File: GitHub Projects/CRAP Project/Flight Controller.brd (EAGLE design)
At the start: 40 x 95 mm, 138 parts, among them J1 2POS_SCREWTERM, J101 2POS_SCREWTERM, J2 4POS_SCREWTERM, J3 4POS_SCREWTERM, J4 4POS_SCREWTERM, J5 4POS_SCREWTERM, Q101 IPD042P03L3G, Q102 IPD042P03L3G, Q1101 PMF170XP, Q1102 DMG4800LSD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

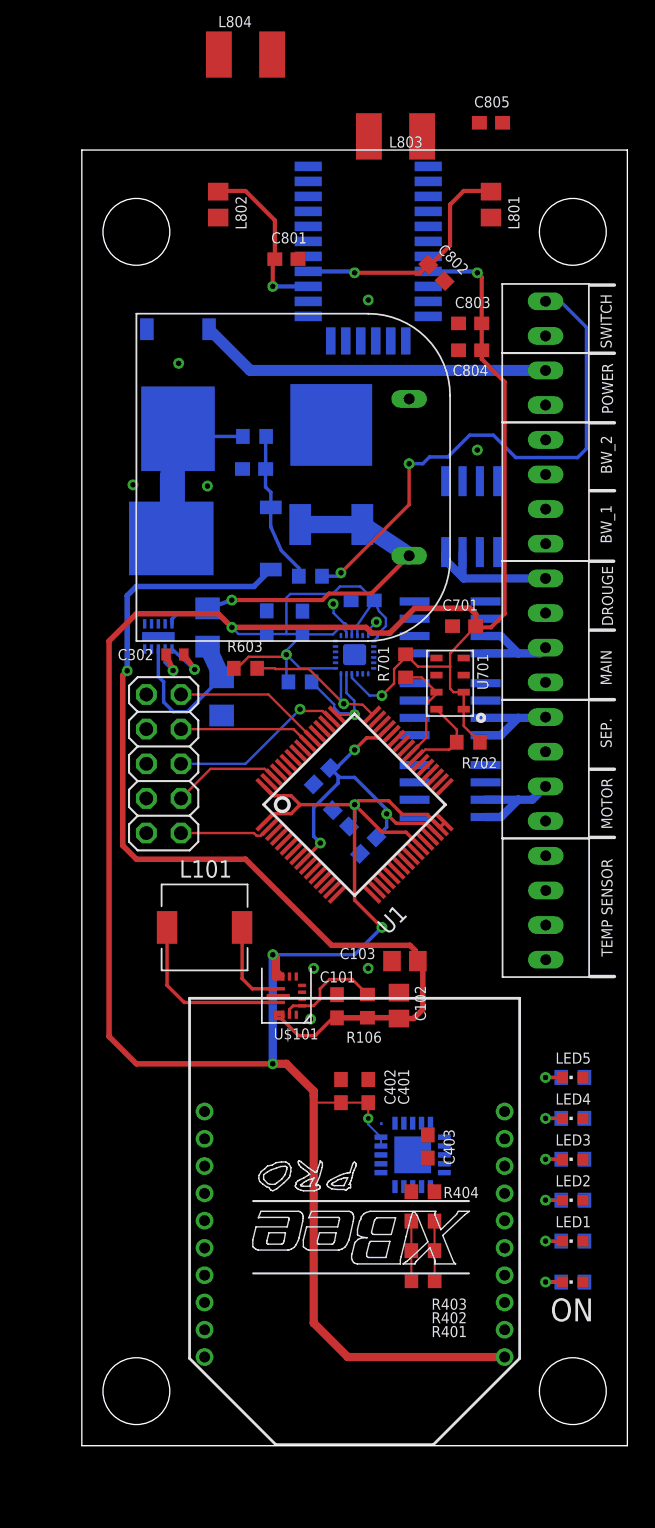
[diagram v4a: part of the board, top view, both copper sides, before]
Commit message: Minor Changes to some routing
Having problems with using the alternate grid.  Routing engine will not
allow me to route on the alternate grid, which has stopped progress for
the time being.
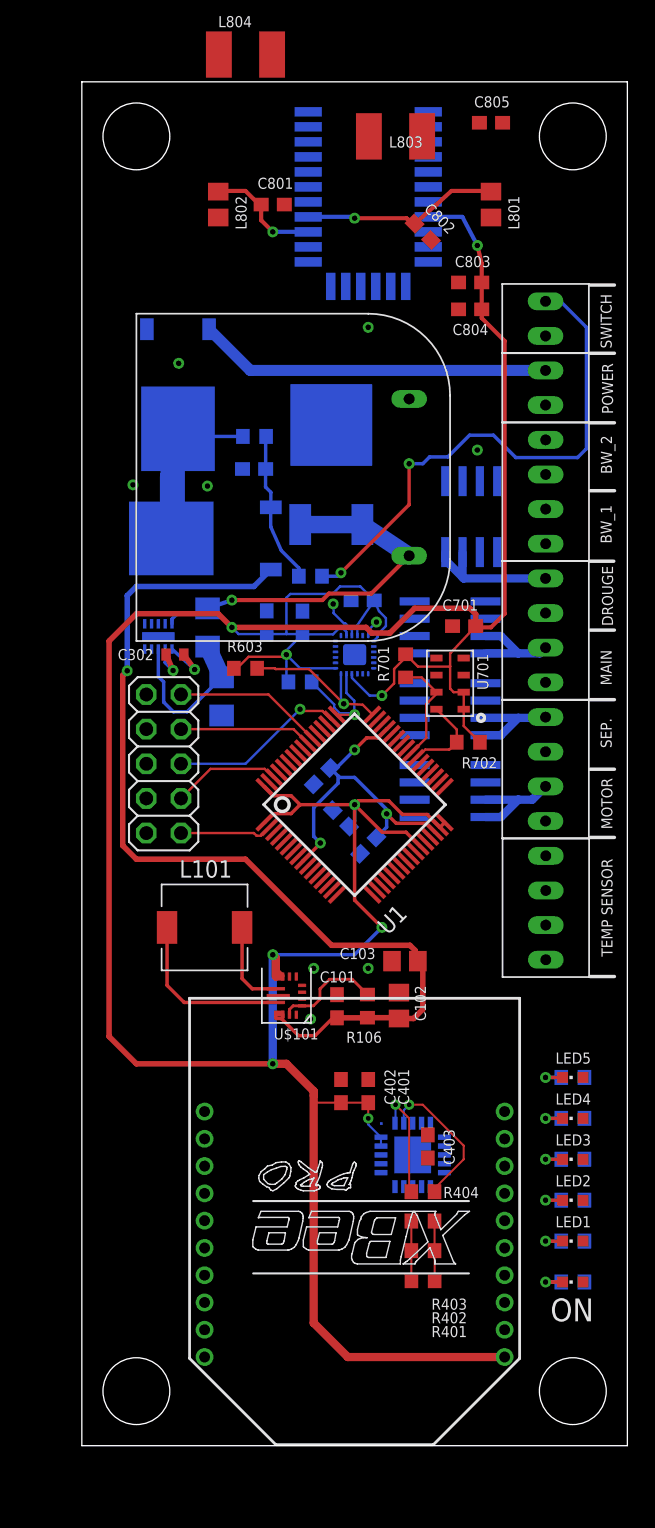
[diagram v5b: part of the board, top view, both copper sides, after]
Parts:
- U1: value (none) -> G55J19
- U301: value (none) -> LTC3225
- U601: value (none) -> MPU9250
- U701: value (none) -> MS5611
- moved C801 4.12 mm to (14.0, 91.0)
- moved U$801 4.00 mm to (21.0, 85.0)
- moved C802 3.16 mm to (25.0, 89.0)
- moved C803 3.00 mm to (28.5, 85.3)
- moved C804 3.00 mm to (28.5, 83.3)
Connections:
- new net BREAKWIRE1:+3V3: R901.2
- new net BREAKWIRE2:+3V3: R1001.2
- new net HIGH_G1:+3V3: C201.1, C202.1, C203.1, U201.P1, U201.P14, U201.P15
- net +3V3: no longer C201.1, C202.1, C203.1, R1001.2, R901.2, U201.P1, U201.P14, U201.P15
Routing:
- net RTD:N$5: track 0.00 -> 11.0 mm, vias 0 -> 1
- net RTD:N$1: track 4.37 -> 12.6 mm, vias 0 -> 1
- net GPS1:N$3: track 12.6 -> 8.57 mm
- net GPS1:N$2: track 17.7 -> 14.5 mm
- net +3V3: track 262.8 -> 265.9 mm
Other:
- board size 40 x 95 mm -> 40 x 100 mm

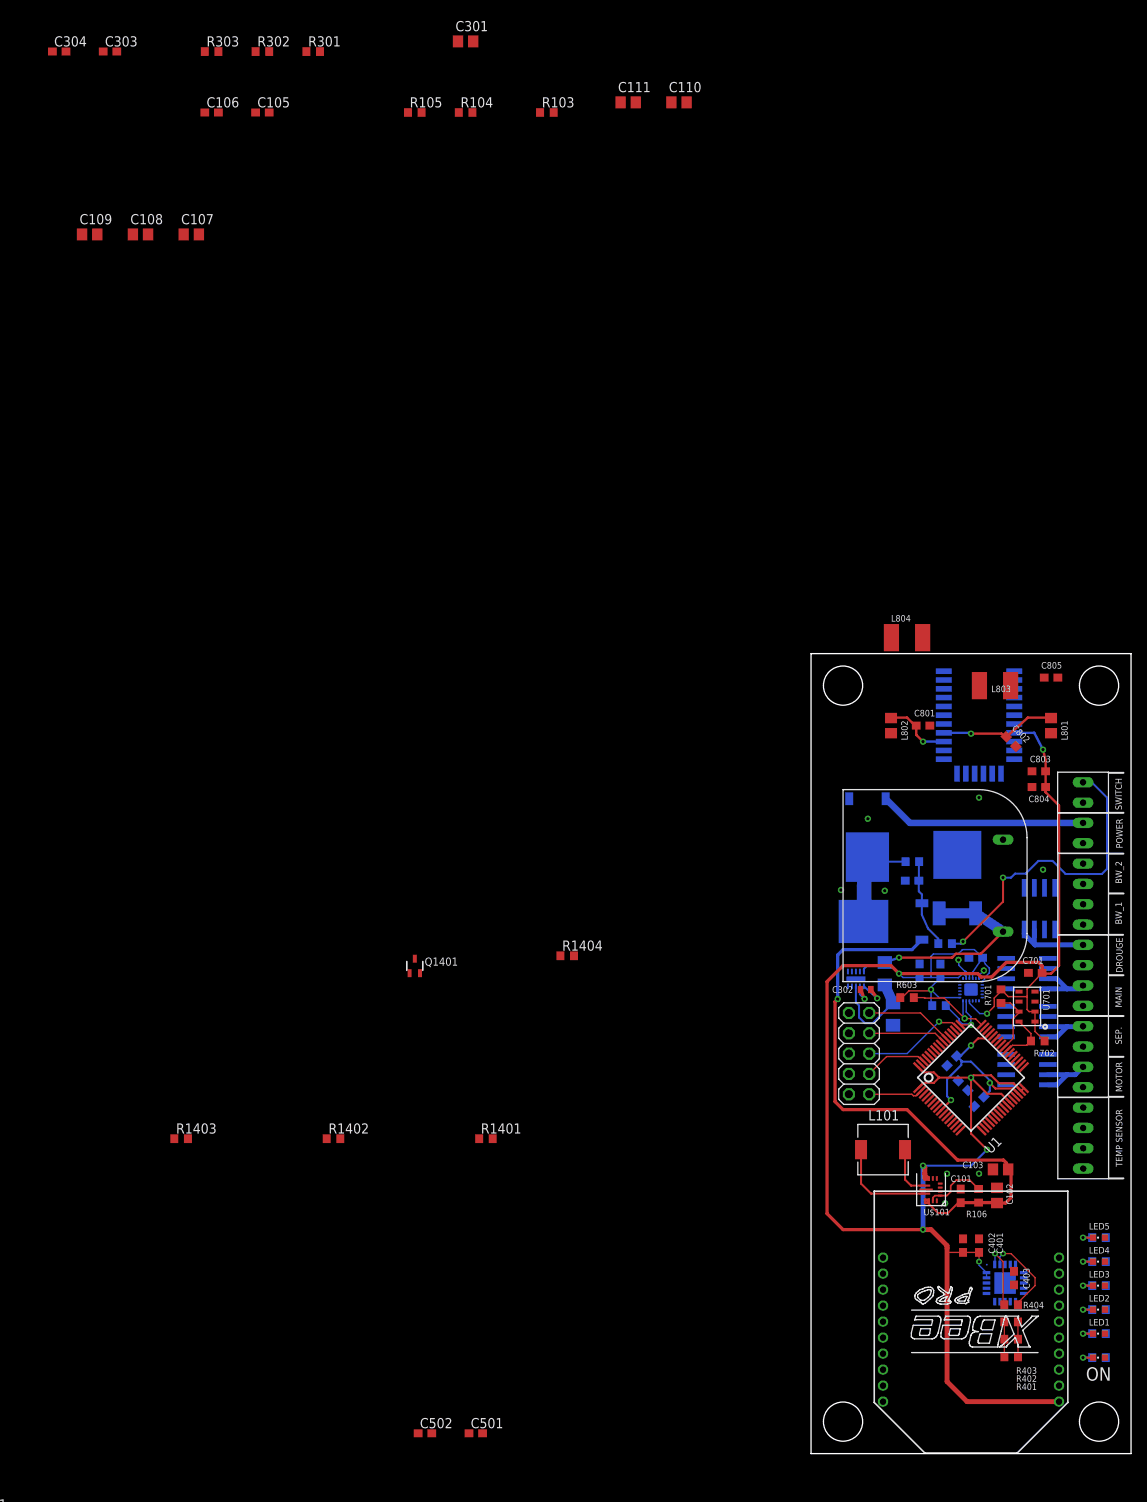
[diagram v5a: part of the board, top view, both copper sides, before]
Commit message: Major revisions
1. Made board 30mm taller to allow for more space in cramped enviroment.
Deemed absolutely critical.
2. Majorly changed the power turn-on and turn-off MOSFETs design and
location to clear up room in the mid-board area
3. Moved the super capacitor nearer to the top of the extended section,
and also made it have a verticle orientation; should allow for better
handling of vertical Gs
4. Moved the super-capacitor charging circuitry in the extra space under
the super-cap.  Fits nicely in a small area now.
5. Created Vishay.lbr, Adafruit.lbr, nkk.lbr, and semtech.lbr
6. Added common SMT pads to Semtech.lbr and Vishay.lbr
7. Created MOSFETs in Vishay.lbr
8.Created MOSFETs in semtech.lbr
9. Completely routed the GPS and passives; just needs UART connections
to the uC now
10. Changed the DRC (Design Rules) to better reflect the capabilities of
Advanced Circuit's $33/board abilities.  Changes are mostly downsizing
the rules to 7mil of smallest hole, trace, and spacing between copper to
copper
11. Modified all vias in tight locations and low power consumption roles
to be a 7mil (0.18mm, rounded) drill hole
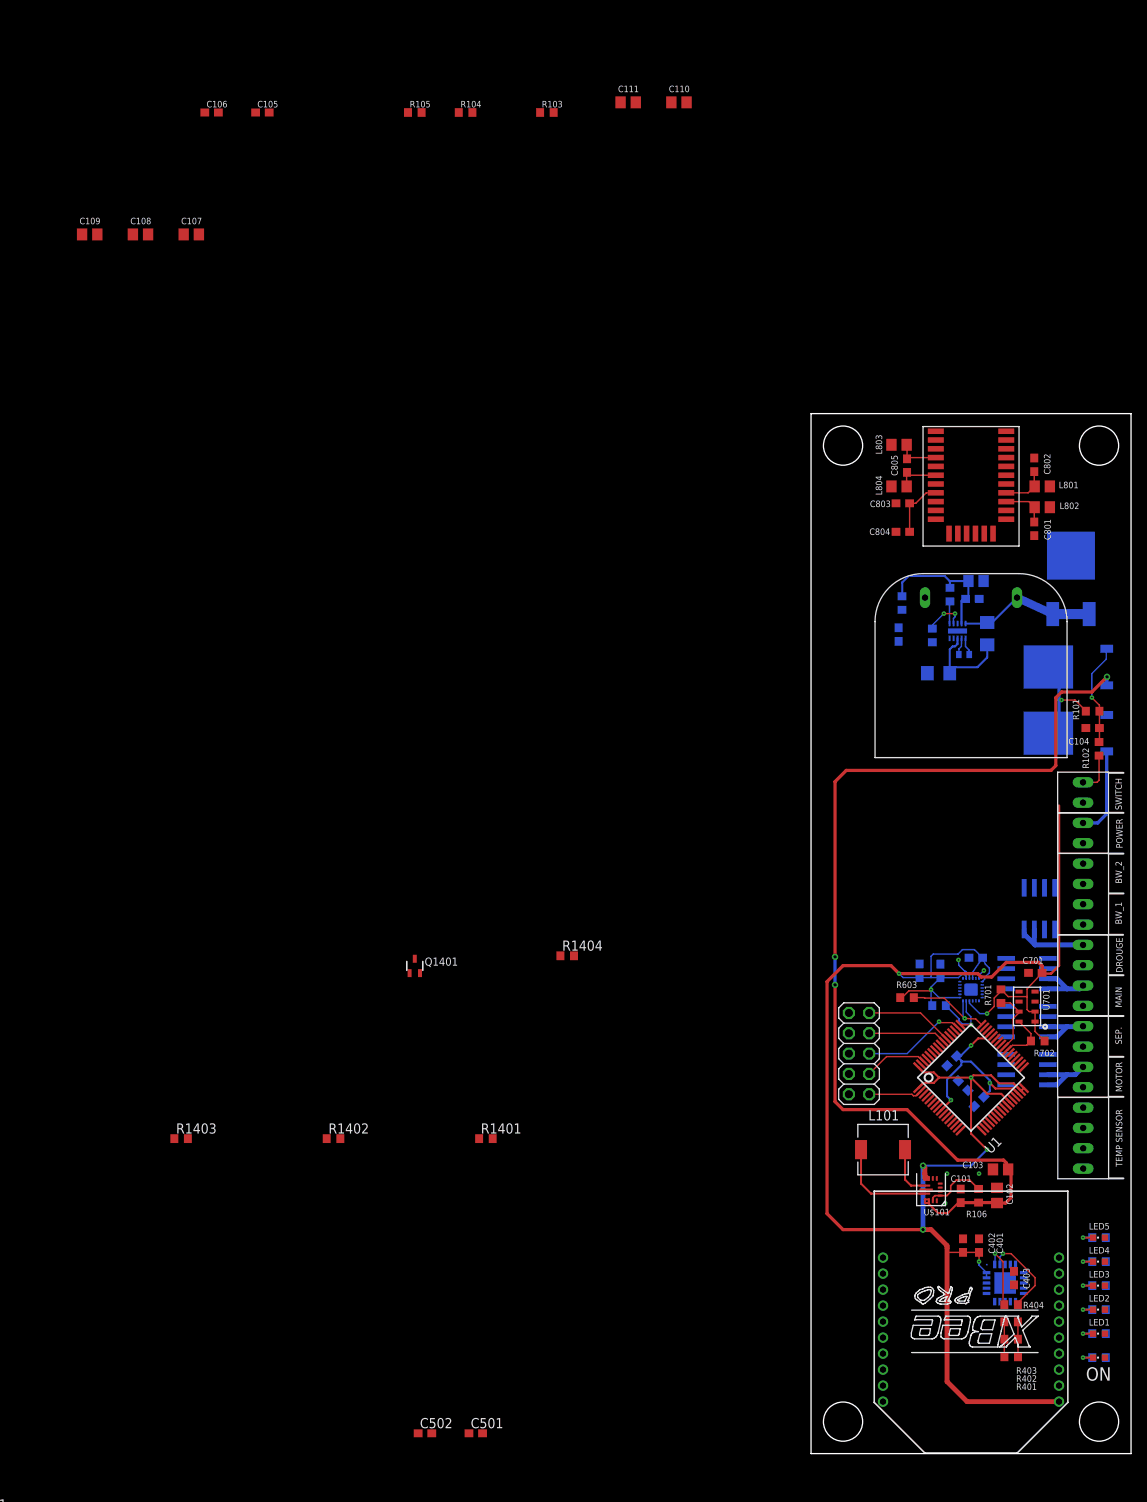
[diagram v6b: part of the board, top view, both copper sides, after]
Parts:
- L803, L804: device rcl:L1812 -> rcl:R0805
- moved C304 127.7 mm to (10.9, 102.4), flipped to the bottom, turned to 270 degrees
- moved C303 127.7 mm to (20.2, 106.8), flipped to the bottom, turned to 180 degrees
- moved R303 115.9 mm to (15.2, 102.3), flipped to the bottom, turned to 90 degrees
- moved R302 105.6 mm to (11.4, 106.3), flipped to the bottom, turned to 90 degrees
- moved R301 104.6 mm to (17.4, 107.4), flipped to the bottom, turned to 90 degrees
- moved C301 92.9 mm to (20.6, 109.1), flipped to the bottom, turned to 180 degrees
- moved U301 45.3 mm to (17.3, 103.8)
- moved C306 44.4 mm to (22.0, 102.5)
- moved C302 43.6 mm to (19.1, 99.9), flipped to the bottom, turned to 0 degrees
- moved C307 43.0 mm to (15.9, 97.5), turned to 0 degrees
- moved D301 40.0 mm to (32.5, 109.7)
- moved Q102 39.3 mm to (32.2, 98.3)
- moved C803 37.6 mm to (11.5, 118.8)
- moved C305 36.2 mm to (20.0, 107.0), turned to 180 degrees
- moved C804 36.1 mm to (11.5, 115.2)
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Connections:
- net DCDC_REGULATOR:N$2 renamed DCDC_REGULATOR:N$1
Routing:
- net DCDC_REGULATOR:VIN: track 72.1 -> 127.3 mm, vias 1 -> 3
- net DCDC_REGULATOR:N$6: track 39.1 -> 5.19 mm, vias 2 -> 0
- net VCC_IN: track 25.9 -> 11.2 mm
- net +3V3: track 265.9 -> 280.0 mm, vias 9 -> 8
- net ORDNANCE_POWER:N$3: track 28.2 -> 17.3 mm, vias 1 -> 0
- net GPS1:N$2: track 14.5 -> 5.75 mm, vias 1 -> 0
- net DCDC_REGULATOR:N$1: track 21.3 -> 12.9 mm, vias 0 -> 1
- net GPS1:N$4: track 0.00 -> 5.75 mm
- net GPS1:N$1: track 0.00 -> 5.55 mm
- net ORDNANCE_POWER:N$6: track 0.00 -> 5.20 mm, vias 0 -> 2
- net GPS1:N$3: track 8.57 -> 5.74 mm, vias 1 -> 0
- net ORDNANCE_POWER:N$5: track 0.00 -> 2.78 mm
- net DCDC_REGULATOR:N$4: track 11.1 -> 12.8 mm, vias 0 -> 1
- net ORDNANCE_POWER:N$1: track 3.59 -> 2.21 mm, vias 1 -> 0
- net ORDNANCE_POWER:N$2: track 3.09 -> 2.15 mm, vias 1 -> 0
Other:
- board size 40 x 100 mm -> 40 x 130 mm

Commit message: Routing of high-g IMU, regular IMU, firing circuits
1. Chose communication lines for all sensors and memory to the uC
2. Routed 100% the MPU9250
3. Routed 100% the high-g accelerometer
4. Routed 100% the breakwire circuits
5. Routed 75% of the firing circuits
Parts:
- removed R1: 10k, rcl:R0603
- moved R1105 432.5 mm to (37.2, 62.3), flipped to the bottom, turned to 270 degrees
- moved R1205 375.6 mm to (37.2, 57.2), flipped to the bottom, turned to 270 degrees
- moved R1305 320.8 mm to (37.2, 52.3), flipped to the bottom, turned to 270 degrees
- moved C203 258.6 mm to (15.8, 66.3), turned to 180 degrees
- moved C202 258.5 mm to (24.8, 64.5), turned to 270 degrees
- moved U201 250.2 mm to (20.0, 70.0), turned to 180 degrees
- moved C201 249.3 mm to (15.3, 64.0), turned to 180 degrees
- moved R1405 195.4 mm to (37.2, 47.1), flipped to the bottom, turned to 270 degrees
- moved D901 177.9 mm to (30.1, 70.0), flipped to the bottom
- moved D1001 175.8 mm to (30.1, 71.5), flipped to the bottom
- moved C1001 175.5 mm to (37.2, 72.5), flipped to the bottom, turned to 270 degrees
- moved C901 174.8 mm to (37.2, 67.3), flipped to the bottom, turned to 270 degrees
- moved R901 164.5 mm to (26.7, 70.4), flipped to the bottom
- moved R1001 162.9 mm to (26.7, 72.5), flipped to the bottom
- moved MEMORY1:U1 140.3 mm to (11.1, 78.0), flipped to the bottom, turned to 270 degrees
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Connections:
- removed net HIGH_G1:+3V3: C201.1, C202.1, C203.1, U201.P1, U201.P14, U201.P15
- removed net HIGH_G1:CS: U201.P8
- removed net HIGH_G1:SCL/SPC: U201.P4
- removed net HIGH_G1:SDA/SDI: U201.P6
- removed net MEMORY1:+3V3: MEMORY1:C1.1, MEMORY1:U1.2
- removed net MEMORY1:GND: MEMORY1:C1.2, MEMORY1:U1.10
- removed net MPU9250_SCL: R602.1, U1.49, U601.23
- removed net MPU9250_SDA: R603.1, U1.48, U601.24
- removed net N$14: R1.2, U601.9
- removed net N$20: U1.8
- removed net N$21: U1.17
- removed net RTD:!CS: U$401.13
- removed net RTD:SCLK: U$401.12
- removed net RTD:SDI: U$401.11
- removed net RTD:SDO: U$401.14
- new net IMU_SCL: R602.1, U1.49, U201.P4, U601.23
- new net IMU_SDA: R603.1, U1.48, U201.P6, U601.24
- new net MEM_!CS: MEMORY1:U1.7, U1.15
- new net MEM_MISO: MEMORY1:U1.8, U1.4
- new net MEM_MOSI: MEMORY1:U1.15, U1.5
- new net MEM_SCK: MEMORY1:U1.16, U1.57
- new net RTD_!CS: U$401.13, U1.18
- new net RTD_MISO: U$401.14, U1.8
- new net RTD_MOSI: U$401.11, U1.17
- new net RTD_SCK: U$401.12, U1.22
- net +3V3: now also C201.1, C202.1, C203.1, MEMORY1:C1.1, MEMORY1:U1.2, U201.P1, U201.P14, U201.P15, U201.P8, U601.9
- net GND: now also MEMORY1:C1.2, MEMORY1:U1.10; no longer R1.1
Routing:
- net +12V: track 0.00 -> 40.3 mm
- net IMU_SDA: track 0.00 -> 30.8 mm, vias 0 -> 4
- net IMU_SCL: track 0.00 -> 28.0 mm, vias 0 -> 2
- net MPU9250_SDA: track 12.1 -> 0.00 mm, vias 1 -> 0
- net MPU9250_SCL: track 8.85 -> 0.00 mm, vias 1 -> 0
- net FIRING_CIRCUIT3:N$1: track 0.00 -> 8.71 mm
- net FIRING_CIRCUIT2:N$1: track 0.00 -> 8.71 mm
- net FIRING_CIRCUIT4:N$1: track 0.00 -> 8.71 mm
- net FIRING_CIRCUIT1:N$1: track 0.00 -> 8.71 mm
- net +3V3: track 280.0 -> 273.4 mm, vias 8 -> 10
- net N$13: track 0.00 -> 5.85 mm
- net FC1-2: track 7.50 -> 11.0 mm
- net FC1-: track 7.73 -> 11.2 mm
- net N$11: track 0.00 -> 3.43 mm
- net N$10: track 0.00 -> 3.41 mm
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
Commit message: More routing and schematic changes
1. Finished 100% the schematic of all misc. connections that were going
to things, such as all comms, all LED indication pins, and all
enable/disable pins
2. Added FTDI FT232R for serial to USB connectivity
3. Routed the power line for the firing circuit from supercap
4. Routed LED indication
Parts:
- added R304: 10k, resistor:R0603
- LED1, LED2, LED3, LED4, LED5: value (none) -> BLUE
- ON: value (none) -> RED
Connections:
- removed net FC1-1: C1301.1, J3.4, Q1302.7, Q1302.8, R1305.1
- removed net FC1-2: C1201.1, J4.2, Q1202.7, Q1202.8, R1205.1
- removed net FC1-3: C1101.1, J4.4, Q1102.7, Q1102.8, R1105.1
- removed net FIRING_CIRCUIT1:!CONT_EN: Q1401.2, R1404.1
- removed net FIRING_CIRCUIT1:FIRE1: Q1402.2, R1403.2
- removed net FIRING_CIRCUIT1:FIRE2: Q1402.4, R1402.2
- removed net FIRING_CIRCUIT2:!CONT_EN: Q1301.2, R1304.1
- removed net FIRING_CIRCUIT2:FIRE1: Q1302.2, R1303.2
- removed net FIRING_CIRCUIT2:FIRE2: Q1302.4, R1302.2
- removed net FIRING_CIRCUIT3:!CONT_EN: Q1201.2, R1204.1
- removed net FIRING_CIRCUIT3:FIRE1: Q1202.2, R1203.2
- removed net FIRING_CIRCUIT3:FIRE2: Q1202.4, R1202.2
- removed net FIRING_CIRCUIT4:!CONT_EN: Q1101.2, R1104.1
- removed net FIRING_CIRCUIT4:FIRE1: Q1102.2, R1103.2
- removed net FIRING_CIRCUIT4:FIRE2: Q1102.4, R1102.2
- removed net N$10: C901.1, J5.2
- removed net N$12: C1001.1, J5.4
- removed net ORDNANCE_POWER:!SHDN: U301.P4
- new net BW1_STATUS: C901.1, J5.2, U1.46
- new net BW2_STATUS: C1001.1, J5.4, U1.47
- new net FC1_!CONT_EN: Q1401.2, R1404.1, U1.6
- new net FC1_FIRE: Q1402.2, Q1402.4, R1402.2, R1403.2, U1.7
- new net FC2-: C1301.1, J3.4, Q1302.7, Q1302.8, R1305.1, U1.52
- new net FC2_!CONT_EN: Q1301.2, R1304.1, U1.61
- new net FC2_FIRE: Q1302.2, Q1302.4, R1302.2, R1303.2, U1.11
- new net FC3-: C1201.1, J4.2, Q1202.7, Q1202.8, R1205.1, U1.19
- new net FC3_!CONT_EN: Q1201.2, R1204.1, U1.12
- new net FC3_FIRE: Q1202.2, Q1202.4, R1202.2, R1203.2, U1.44
- new net FC4-: C1101.1, J4.4, Q1102.7, Q1102.8, R1105.1, U1.16
- new net FC4_!CONT_EN: Q1101.2, R1104.1, U1.41
- new net FC4_FIRE: Q1102.2, Q1102.4, R1102.2, R1103.2, U1.58
- new net ORD_!SHDN: R304.1, U1.20, U301.P4
- new net USB_RX: U1.37
- new net USB_TX: U1.38
- net +3V3: now also R304.2
- net FC1-: now also U1.56
- net UC_LED1: now also U1.33
- net UC_LED2: now also U1.34
- net UC_LED3: now also U1.35
- net UC_LED4: now also U1.36
- net UC_LED5: now also U1.23
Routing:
- net +12V: track 40.3 -> 95.7 mm, vias 0 -> 5
- net UC_LED1: track 0.00 -> 41.4 mm
- net UC_LED2: track 0.00 -> 39.0 mm
- net UC_LED3: track 0.00 -> 36.6 mm
- net UC_LED4: track 0.00 -> 34.3 mm
- net UC_LED5: track 0.00 -> 23.5 mm, vias 0 -> 2
- net FC4-: track 0.00 -> 11.2 mm
- net FC1-3: track 11.2 -> 0.00 mm
- net FC3-: track 0.00 -> 11.0 mm
- net FC1-2: track 11.0 -> 0.00 mm
- net FC2-: track 0.00 -> 10.7 mm
- net FC1-1: track 10.7 -> 0.00 mm
- net N$10: track 3.41 -> 0.00 mm
- net BW1_STATUS: track 0.00 -> 3.41 mm
- net N$12: track 3.36 -> 0.00 mm
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- added copper zone on layer 16, net +12V
